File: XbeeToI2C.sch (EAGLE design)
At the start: 50 parts, among them Q1 MOSFET-NCHANNELSMD, Q2 MOSFET-NCHANNELSMD, U1 SC18IM700IPW,112, U2 XBEE-1B3, U3 V_REG_LDOSMD

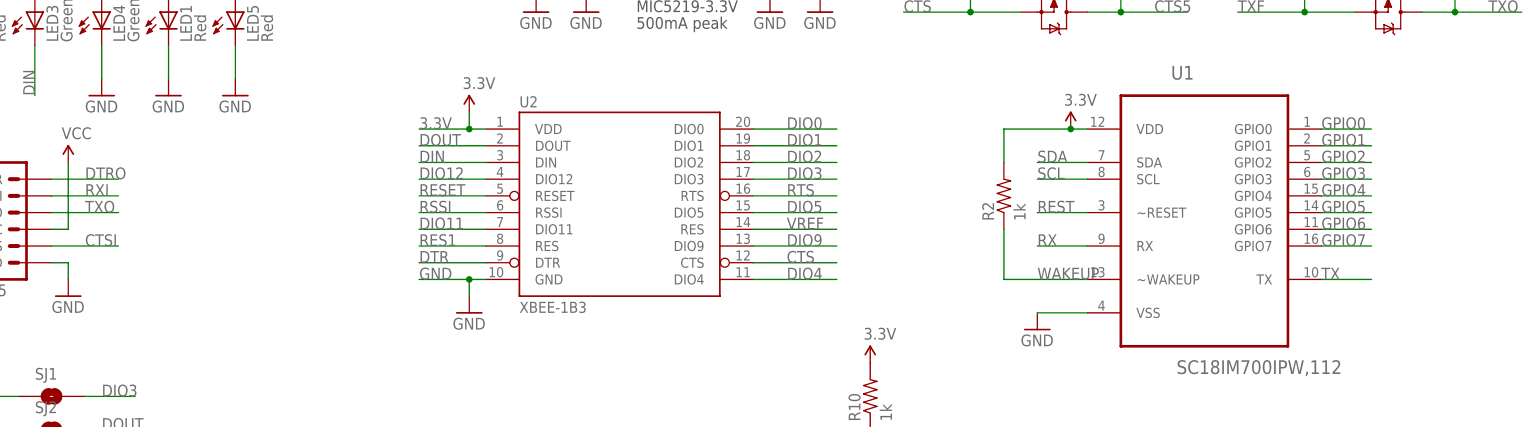
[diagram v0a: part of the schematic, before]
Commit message: Com change
Added resistors to the UART xbee and the out put of the I2C
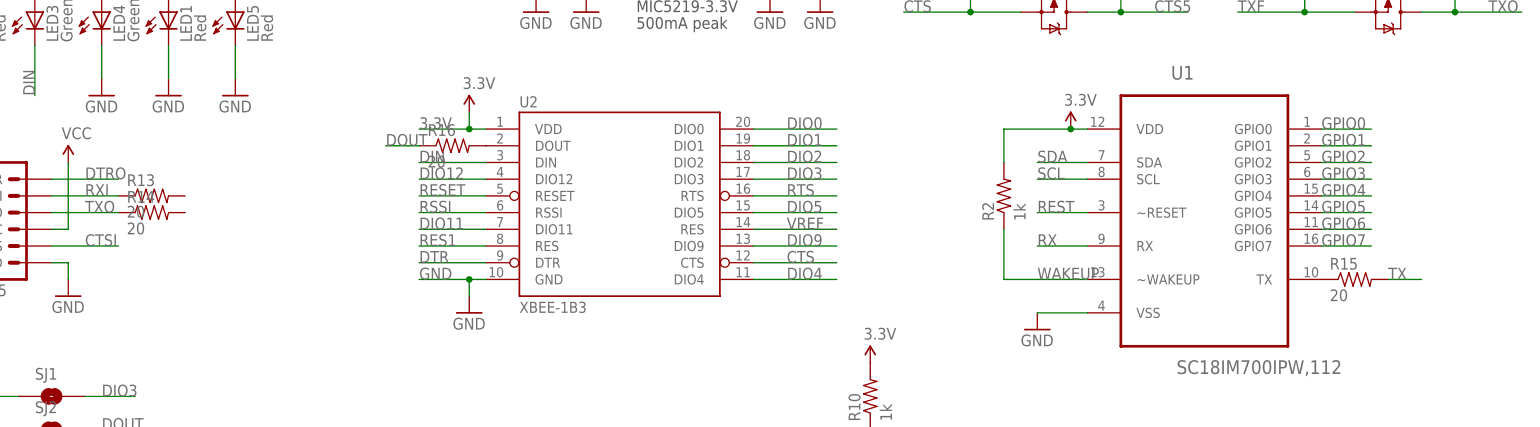
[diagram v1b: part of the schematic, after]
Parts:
- added R13, R14, R15, R16: 20, SparkFun-Resistors:20OHM1/10W1%(0603)SMD
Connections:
- new net N$3: R16.2, U2.DOUT
- new net N$5: R15.1, U1.TX
- net DOUT: now also R16.1; no longer U2.DOUT
- net RXI: now also R13.1
- net TX: now also R15.2; no longer U1.TX
- net TXO: now also R14.1
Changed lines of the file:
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@@
 <part name="P+9" library="SparkFun" deviceset="3.3V" device=""/>
 <part name="GND13" library="SparkFun" deviceset="GND" device=""/>
+<part name="R13" library="SparkFun-Resistors" deviceset="20OHM1/10W1%(0603)" device="SMD" value="20"/>
+<part name="R14" library="SparkFun-Resistors" deviceset="20OHM1/10W1%(0603)" device="SMD" value="20"/>
+<part name="R15" library="SparkFun-Resistors" deviceset="20OHM1/10W1%(0603)" device="SMD" value="20"/>
+<part name="R16" library="SparkFun-Resistors" deviceset="20OHM1/10W1%(0603)" device="SMD" value="20"/>
 </parts>
 <sheets>
@@
 <instance part="P+9" gate="G$1" x="144.78" y="99.06"/>
 <instance part="GND13" gate="1" x="144.78" y="71.12"/>
+<instance part="R13" gate="G$1" x="35.56" y="124.46"/>
+<instance part="R14" gate="G$1" x="35.56" y="121.92"/>
+<instance part="R15" gate="G$1" x="218.44" y="111.76"/>
+<instance part="R16" gate="G$1" x="81.28" y="132.08"/>
 </instances>
 <busses>
@@
 <net name="DOUT" class="0">
 <segment>
-<wire x1="86.36" y1="132.08" x2="76.2" y2="132.08" width="0.1524" layer="91"/>
-<label x="76.2" y="132.08" size="1.778" layer="95"/>
-<pinref part="U2" gate="G$1" pin="DOUT"/>
-</segment>
-<segment>
 <pinref part="SJ2" gate="1" pin="2"/>
 <wire x1="25.4" y1="88.9" x2="33.02" y2="88.9" width="0.1524" layer="91"/>
@@
 <label x="27.94" y="55.88" size="1.778" layer="95"/>
 </segment>
+<segment>
+<pinref part="R16" gate="G$1" pin="1"/>
+<wire x1="76.2" y1="132.08" x2="71.12" y2="132.08" width="0.1524" layer="91"/>
+<label x="71.12" y="132.08" size="1.778" layer="95"/>
+</segment>
 </net>
 <net name="DIN" class="0">
@@
 <label x="25.4" y="124.46" size="1.778" layer="95"/>
 <pinref part="JP5" gate="G$1" pin="RXI"/>
+<pinref part="R13" gate="G$1" pin="1"/>
 </segment>
 <segment>
@@
 <label x="25.4" y="121.92" size="1.778" layer="95"/>
 <pinref part="JP5" gate="G$1" pin="TXO"/>
+<pinref part="R14" gate="G$1" pin="1"/>
 </segment>
 <segment>
@@
 </segment>
 <segment>
-<pinref part="U1" gate="A" pin="TX"/>
-<wire x1="213.36" y1="111.76" x2="220.98" y2="111.76" width="0.1524" layer="91"/>
-<label x="213.36" y="111.76" size="1.778" layer="95"/>
-</segment>
-<segment>
 <pinref part="JP1" gate="B" pin="6"/>
 <wire x1="12.7" y1="58.42" x2="7.62" y2="58.42" width="0.1524" layer="91"/>
 <label x="7.62" y="58.42" size="1.778" layer="95"/>
+</segment>
+<segment>
+<pinref part="R15" gate="G$1" pin="2"/>
+<wire x1="223.52" y1="111.76" x2="228.6" y2="111.76" width="0.1524" layer="91"/>
+<label x="223.52" y="111.76" size="1.778" layer="95"/>
 </segment>
 </net>
@@
 </segment>
 </net>
+<net name="N$3" class="0">
+<segment>
+<pinref part="U2" gate="G$1" pin="DOUT"/>
+<pinref part="R16" gate="G$1" pin="2"/>
+</segment>
+</net>
+<net name="N$5" class="0">
+<segment>
+<pinref part="U1" gate="A" pin="TX"/>
+<pinref part="R15" gate="G$1" pin="1"/>
+</segment>
+</net>
